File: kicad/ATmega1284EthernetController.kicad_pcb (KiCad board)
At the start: 4 copper layers, 100 x 80 mm, 45 parts, among them J1 DC2 9-12V, J2 AVR-ISP-6, J3 DC1 9-12V, J4 RJ45_Amphenol_RJMG1BD3B8K1ANR, J5 PA0-7, J6 PC0-7, J7 PB0-3/PD3-7, J8 SIO, SW1 SELECT, SW2 RESET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

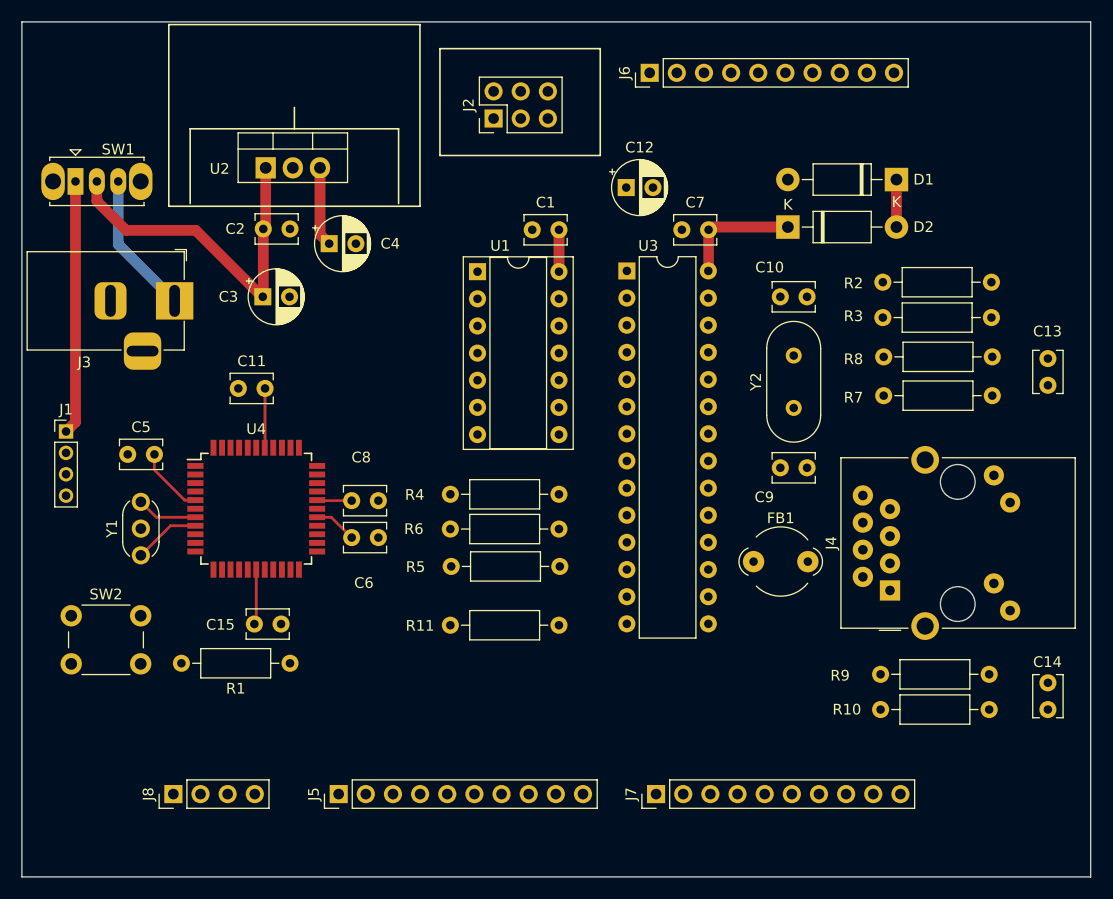
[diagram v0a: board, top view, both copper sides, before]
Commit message: Update ATmega1284EthernetController.kicad_pcb
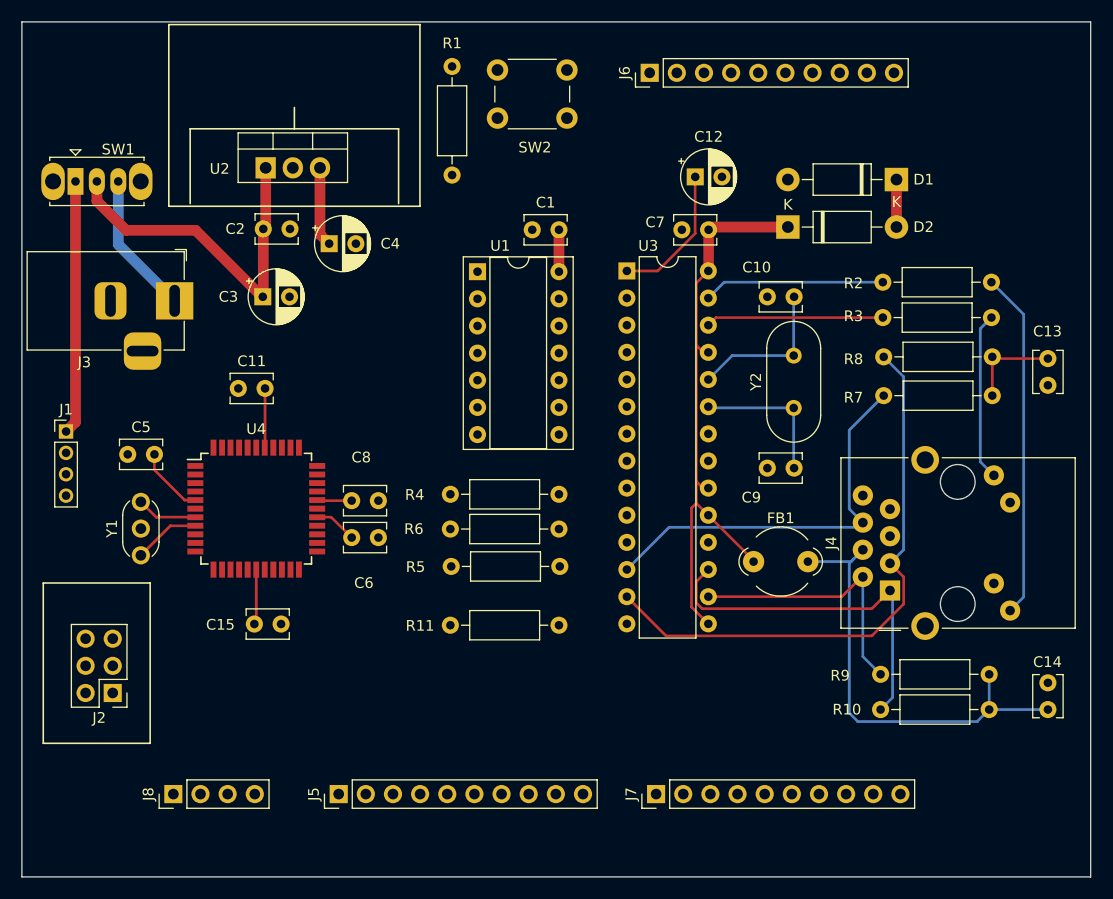
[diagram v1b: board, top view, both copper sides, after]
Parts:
- moved SW2 64.8 mm to (64.5, 24.5)
- moved J2 64.5 mm to (28.5, 82.8), turned to 180 degrees
- moved R1 48.1 mm to (60.2, 34.3), turned to 90 degrees
- moved C12 6.53 mm to (83.0, 34.5)
- moved C9 1.22 mm to (89.8, 61.8)
- moved C10 1.22 mm to (89.8, 45.7)
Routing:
- net Net-(J4-RD+): track 0.00 -> 53.6 mm
- net +3.3V: track 11.4 -> 56.2 mm
- net Net-(J4-TCT): track 0.00 -> 44.1 mm
- net Net-(J4-RD-): track 0.00 -> 37.6 mm
- net Net-(J4-TD+): track 0.00 -> 34.3 mm
- net Net-(J4-PadL4): track 0.00 -> 32.5 mm
- net Net-(J4-TD-): track 0.00 -> 25.0 mm
- net Net-(U3-LEDA): track 0.00 -> 16.9 mm
- net Net-(U3-LEDB): track 0.00 -> 16.6 mm
- net Net-(J4-PadL1): track 0.00 -> 15.7 mm
- net Net-(U3-OSC2): track 0.00 -> 14.5 mm
- net Net-(U3-OSC1): track 0.00 -> 13.9 mm
- net Net-(U3-VCAP): track 0.00 -> 13.1 mm
- net Net-(C13-Pad1): track 0.00 -> 8.90 mm
- net Net-(U3-SI): track 0.00 -> 0.70 mm
- added copper zone on In2.Cu, net +5V
- added copper zone on In1.Cu, net GND

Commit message: Update ATmega1284EthernetController.kicad_pcb
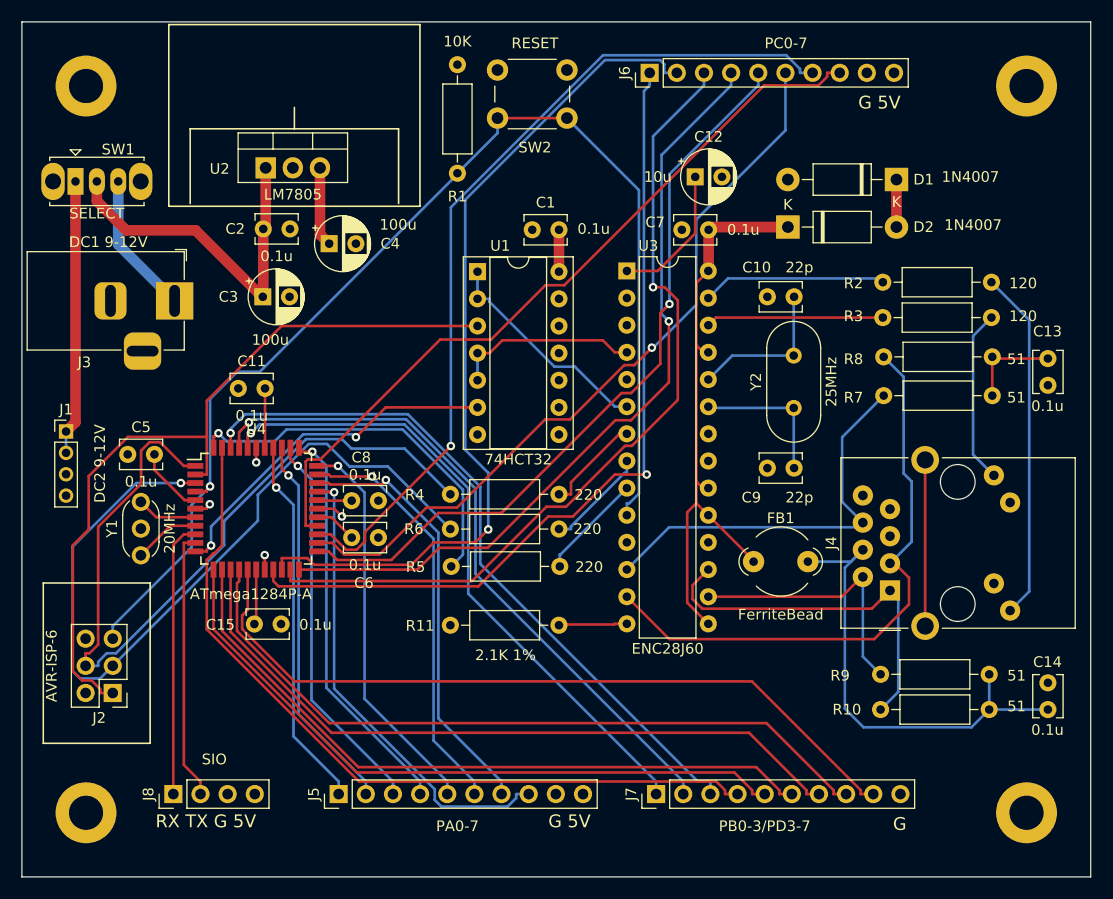
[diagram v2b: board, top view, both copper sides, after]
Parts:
- added REF**: MountingHole_3.2mm_M3_ISO7380_Pad, MountingHole:MountingHole_3.2mm_M3_ISO7380_Pad, F.Cu at (114.0, 26.0)
- added REF**: MountingHole_3.2mm_M3_ISO7380_Pad, MountingHole:MountingHole_3.2mm_M3_ISO7380_Pad, F.Cu at (26.0, 26.0)
- added REF**: MountingHole_3.2mm_M3_ISO7380_Pad, MountingHole:MountingHole_3.2mm_M3_ISO7380_Pad, F.Cu at (114.0, 94.0)
- added REF**: MountingHole_3.2mm_M3_ISO7380_Pad, MountingHole:MountingHole_3.2mm_M3_ISO7380_Pad, F.Cu at (26.0, 94.0)
- U3: value ENC28J60x-SP -> ENC28J60
- moved R1 10.3 mm to (60.8, 24.0), turned to -90 degrees
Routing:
- net Net-(J2-~{RST}): track 0.00 -> 113.6 mm, vias 0 -> 1
- net PC6: track 0.00 -> 80.6 mm, vias 0 -> 1
- net PC1: track 0.00 -> 79.9 mm, vias 0 -> 1
- net PC2: track 0.00 -> 78.6 mm, vias 0 -> 1
- net PC0: track 0.00 -> 78.5 mm, vias 0 -> 1
- net Net-(J2-MOSI): track 0.00 -> 75.4 mm
- net Net-(J2-SCK): track 0.00 -> 75.0 mm, vias 0 -> 1
- net PB3: track 0.00 -> 73.9 mm
- net PC3: track 0.00 -> 73.8 mm, vias 0 -> 1
- net Net-(J2-MISO): track 0.00 -> 72.4 mm
- net PC7: track 0.00 -> 72.3 mm
- net PD7: track 0.00 -> 71.4 mm
- net PC4: track 0.00 -> 71.1 mm, vias 0 -> 1
- net PC5: track 0.00 -> 70.8 mm, vias 0 -> 1
- net PD6: track 0.00 -> 69.4 mm
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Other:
- board text added: "G"
- board text added: "G 5V"
- board text added: "RX TX G 5V"
